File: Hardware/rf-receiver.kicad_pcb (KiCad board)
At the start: 4 copper layers, 90.8 x 50 mm, 160 parts, among them CON1 FPC_6POS, IC1 ATSAMD21G18A-AU, IC2 AD9954, IC3 74LVC74, J1 Conn_01x05_Female, J2 Conn_Coaxial, J3 USB_B_Micro, P1 ROT_ENC, SW1 BTN1, SW2 BTN2, SW3 BTN3, U1 74HC14, U10 TPS62173DSG, U11 MIC5504-1.8YM5, U12 MIC5504-1.8YM5, U2 RC1602A, U3 TXB0108PWR, U4 MIC5504-3.3YM5, U5 OPA300, U7 Transformer, U8 NE5532, U9 74CBTLV3253, Y1 Crystal_Small

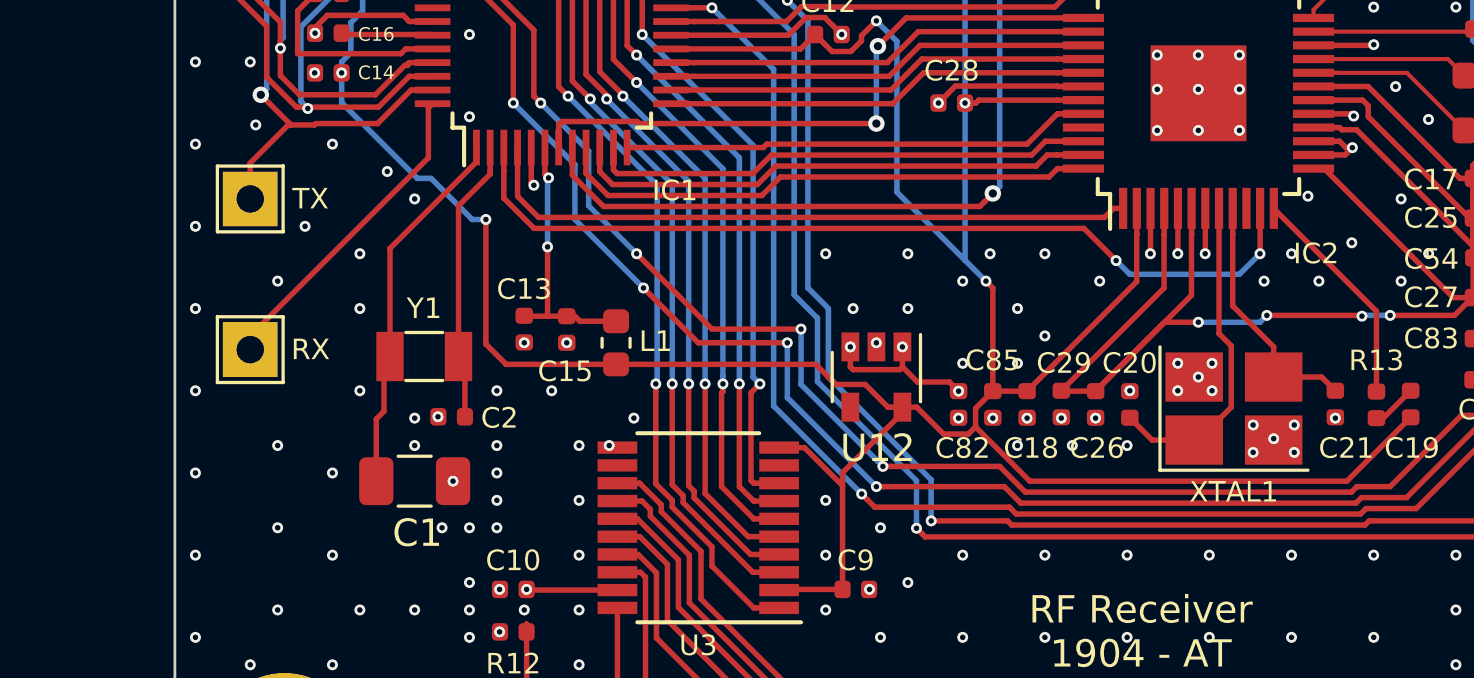
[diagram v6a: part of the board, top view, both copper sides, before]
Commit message: Added 3D models...
25MHz oscillator -> footprint no longer handsoldering variant.
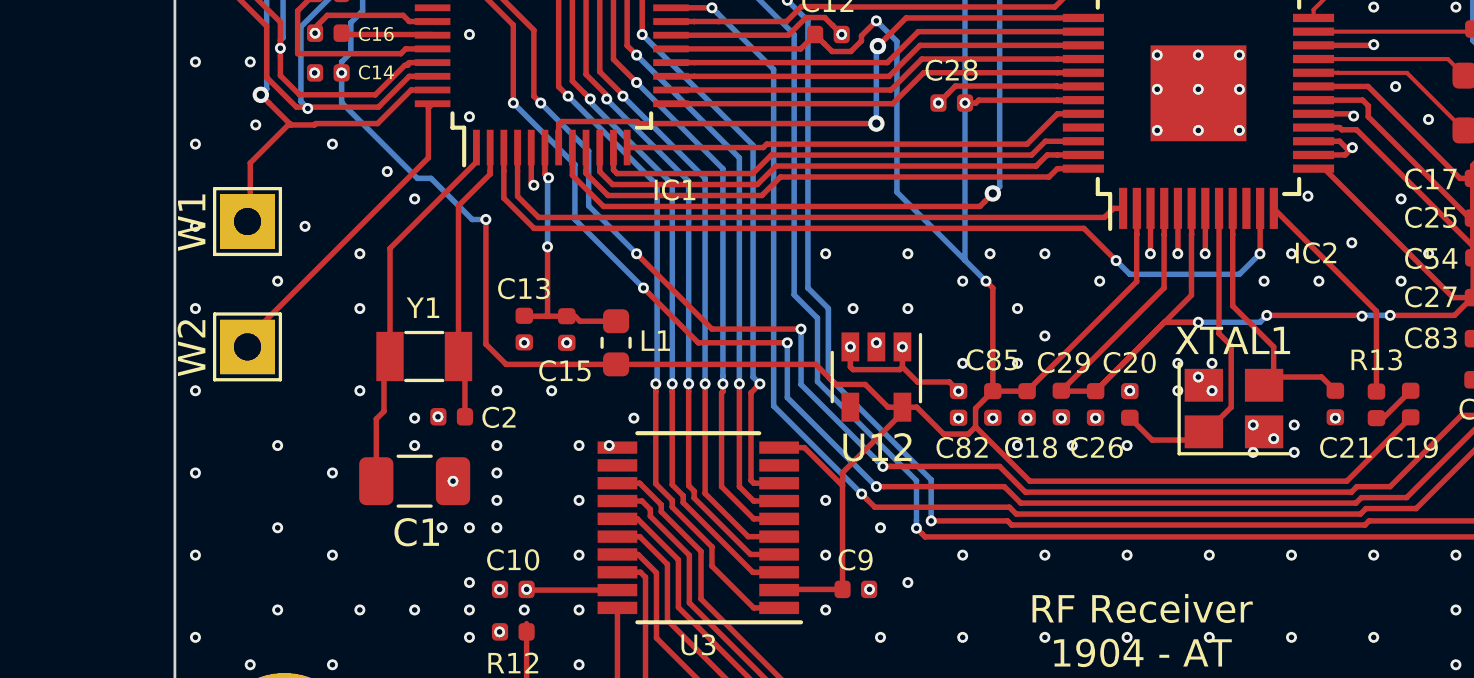
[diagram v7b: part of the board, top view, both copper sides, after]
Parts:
- removed REF**: Hammond_1550B, athir:Hammond_1550B
- removed RX: RX, TestPoint:TestPoint_THTPad_2.0x2.0mm_Drill1.0mm
- removed TX: TX, TestPoint:TestPoint_THTPad_2.0x2.0mm_Drill1.0mm
- added W1: TX, TestPoint:TestPoint_THTPad_2.0x2.0mm_Drill1.0mm, F.Cu at (69.9, 89.8)
- added W2: RX, TestPoint:TestPoint_THTPad_2.0x2.0mm_Drill1.0mm, F.Cu at (69.9, 94.4)
- XTAL1: footprint Crystal:Crystal_SMD_3225-4Pin_3.2x2.5mm_HandSoldering -> Crystal:Crystal_SMD_3225-4Pin_3.2x2.5mm

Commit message: HW rev1
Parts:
- removed PSU+1: PSU+, TestPoint:TestPoint_THTPad_2.0x2.0mm_Drill1.0mm
- removed PSU-1: PSU-, TestPoint:TestPoint_THTPad_2.0x2.0mm_Drill1.0mm
- added +: PSU+, TestPoint:TestPoint_THTPad_2.0x2.0mm_Drill1.0mm, F.Cu at (98.8, 65.5)
- added -: PSU-, TestPoint:TestPoint_THTPad_2.0x2.0mm_Drill1.0mm, F.Cu at (108.0, 65.5)
- added C55: C_Small, Capacitor_SMD:C_0603_1608Metric, F.Cu at (88.4, 74.8)
- C1: footprint Resistor_SMD:R_1206_3216Metric -> Capacitor_SMD:C_0603_1608Metric
- C10, C11, C12, C13, C14, C15, C16, C17, C18, C19, C2, C20, C21, C22, C23, C24, C25, C26, C27, C28, C29, C3, C30, C31, C32, C33, C34, C35, C36, C37, C38, C39, C4, C40, C41, C42, C43, C44, C45, C46, C47, C48, C49, C5, C50, C51, C53, C54, C56, C57, C59, C6, C61, C62, C63, C65, C66, C67, C68, C69, C7, C70, C71, C72, C73, C74, C75, C77, C79, C8, C80, C82, C83, C85, C9: footprint Capacitor_SMD:C_0402_1005Metric -> Capacitor_SMD:C_0603_1608Metric
- J3: value USB_B_Micro -> USB_C_Receptacle; footprint Connector_USB:USB_Micro-B_Molex-105017-0001 -> athir:DX07S024JJ
- L2, L3, L4, L5, L6, L7: footprint Inductor_SMD:L_0402_1005Metric -> Inductor_SMD:L_0603_1608Metric
- R1, R10, R11, R12, R13, R16, R18, R19, R2, R20, R22, R23, R24, R26, R27, R29, R3, R30, R31, R32, R33, R4, R5, R6, R7, R8, R9: footprint Resistor_SMD:R_0402_1005Metric -> Resistor_SMD:R_0603_1608Metric
- moved C76 3.39 mm to (94.2, 76.9), turned to 180 degrees
- moved C40 1.75 mm to (117.6, 67.8)
- moved C34 1.71 mm to (111.2, 67.8)
- moved C37 1.55 mm to (114.4, 67.8)
- moved TP6 1.52 mm to (153.0, 89.5)
- moved L6 1.44 mm to (117.6, 69.6)
- moved L7 1.42 mm to (118.2, 74.6)
- moved C41 1.40 mm to (118.2, 76.2)
- moved L2 1.39 mm to (111.2, 69.6)
- moved L4 1.20 mm to (114.4, 69.6)
- moved W1 0.83 mm to (70.0, 89.0), turned to 0 degrees
- moved CON1 0.82 mm to (79.2, 68.8)
- moved J2 0.76 mm to (140.2, 65.7)
- moved J3 0.75 mm to (91.0, 65.0)
- moved L5 0.66 mm to (115.0, 74.6)
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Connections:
- CON1 pad 7: Net-(CON1-Pad7) -> (no net)
- R3 pad 2: Net-(J3-Pad1) -> Net-(C55-Pad1)
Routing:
- net GND: track 40.3 -> 60.9 mm, vias 516 -> 384
- net Net-(C55-Pad1): track 0.00 -> 14.7 mm, vias 0 -> 2
- net Net-(J3-Pad1): track 9.22 -> 0.00 mm
- net +1V8: track 163.8 -> 168.2 mm
- net /USB_D-: track 17.9 -> 21.6 mm, vias 0 -> 3
- net Net-(C33-Pad2): track 16.1 -> 18.7 mm
- net +12V: track 54.6 -> 57.0 mm
- net /AD9954sheet/IOUT-: track 26.9 -> 29.3 mm
- net /AD9954sheet/IOUT+: track 23.3 -> 21.3 mm
- net /UART_TX: track 34.1 -> 35.9 mm
- net /JTAGConn58895F8D/SWDIO: track 34.1 -> 36.0 mm
- net /JTAGConn58895F8D/MCU_RESET: track 27.8 -> 29.6 mm
- net Net-(C33-Pad1): track 18.1 -> 19.7 mm
- net Net-(C34-Pad2): track 5.85 -> 6.98 mm
- net /JTAGConn58895F8D/SWCLK: track 34.3 -> 35.3 mm
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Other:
- net class Default: clearance 0.2 -> 0.15
- rule trace_clearance: 0.2 -> 0.15
- board text added: "RF Receiver 1912- AT"
- board text removed: "RF Receiver 1904 - AT"
